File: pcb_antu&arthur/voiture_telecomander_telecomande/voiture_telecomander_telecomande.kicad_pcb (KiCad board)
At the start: 2 copper layers, 100 x 85 mm, 31 parts, among them J1 batterie, J2 Ecran 7 segments, J3 bouton1, J4 bouton2, J5 interrupteur, J6 led RGB, U1 ESP32-C6-DEVKITC-1-N8, U2 COM-09032 (joystick)

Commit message: mise a jour PCB antu_arthur
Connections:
- J6 pad 4: GND -> +3V3
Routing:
- net +3V3: track 177.7 -> 206.4 mm
- net GND: track 265.5 -> 261.3 mm
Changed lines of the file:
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@@
 		)
 		(embedded_fonts no)
-		(model "${KICAD9_3DMODEL_DIR}/Resistor_THT.3dshapes/R_Axial_DIN0207_L6.3mm_D2.5mm_P10.16mm_Horizontal.step"
+		(model "${KIPRJMOD}/3d/R_Axial_DIN0207_L6.3mm_D2.5mm_P10.16mm_Horizontal.step"
 			(offset
 				(xyz 0 0 0)
@@
 		)
 		(embedded_fonts no)
-		(model "${KICAD9_3DMODEL_DIR}/Resistor_THT.3dshapes/R_Axial_DIN0207_L6.3mm_D2.5mm_P10.16mm_Horizontal.step"
+		(model "${KIPRJMOD}/3d/R_Axial_DIN0207_L6.3mm_D2.5mm_P10.16mm_Horizontal.step"
 			(offset
 				(xyz 0 0 0)
@@
 		)
 		(embedded_fonts no)
-		(model "${KICAD9_3DMODEL_DIR}/Capacitor_THT.3dshapes/C_Radial_D4.0mm_H7.0mm_P1.50mm.step"
+		(model "${KIPRJMOD}/3d/C_Radial_D4.0mm_H7.0mm_P1.50mm.step"
 			(offset
 				(xyz 0 0 0)
@@
 		)
 		(embedded_fonts no)
-		(model "${KICAD9_3DMODEL_DIR}/Resistor_THT.3dshapes/R_Axial_DIN0207_L6.3mm_D2.5mm_P10.16mm_Horizontal.step"
+		(model "${KIPRJMOD}/3d/R_Axial_DIN0207_L6.3mm_D2.5mm_P10.16mm_Horizontal.step"
 			(offset
 				(xyz 0 0 0)
@@
 		)
 		(embedded_fonts no)
-		(model "${KICAD9_3DMODEL_DIR}/Resistor_THT.3dshapes/R_Axial_DIN0207_L6.3mm_D2.5mm_P10.16mm_Horizontal.step"
+		(model "${KIPRJMOD}/3d/R_Axial_DIN0207_L6.3mm_D2.5mm_P10.16mm_Horizontal.step"
 			(offset
 				(xyz 0 0 0)
@@
 		)
 		(embedded_fonts no)
-		(model "${KICAD9_3DMODEL_DIR}/Capacitor_THT.3dshapes/C_Radial_D4.0mm_H7.0mm_P1.50mm.step"
+		(model "${KIPRJMOD}/3d/C_Radial_D4.0mm_H7.0mm_P1.50mm.step"
 			(offset
 				(xyz 0 0 0)
@@
 		)
 		(embedded_fonts no)
-		(model "${KICAD9_3DMODEL_DIR}/Capacitor_THT.3dshapes/C_Radial_D4.0mm_H7.0mm_P1.50mm.step"
+		(model "${KIPRJMOD}/3d/C_Radial_D4.0mm_H7.0mm_P1.50mm.step"
 			(offset
 				(xyz 0 0 0)
@@
 		)
 		(embedded_fonts no)
-		(model "${KICAD9_3DMODEL_DIR}/Capacitor_THT.3dshapes/C_Radial_D4.0mm_H7.0mm_P1.50mm.step"
+		(model "${KIPRJMOD}/3d/C_Radial_D4.0mm_H7.0mm_P1.50mm.step"
 			(offset
 				(xyz 0 0 0)
@@
 		)
 		(embedded_fonts no)
-		(model "${KICAD9_3DMODEL_DIR}/Resistor_THT.3dshapes/R_Axial_DIN0207_L6.3mm_D2.5mm_P10.16mm_Horizontal.step"
+		(model "${KIPRJMOD}/3d/R_Axial_DIN0207_L6.3mm_D2.5mm_P10.16mm_Horizontal.step"
 			(offset
 				(xyz 0 0 0)
@@
 		)
 		(embedded_fonts no)
-		(model "${KICAD9_3DMODEL_DIR}/Connector_JST.3dshapes/JST_XH_B2B-XH-A_1x02_P2.50mm_Vertical.step"
+		(model "${KIPRJMOD}/3d/JST_XH_B2B-XH-A_1x02_P2.50mm_Vertical.step"
 			(offset
 				(xyz 0 0 0)
@@
 		)
 		(embedded_fonts no)
-		(model "${KICAD9_3DMODEL_DIR}/Resistor_THT.3dshapes/R_Axial_DIN0207_L6.3mm_D2.5mm_P10.16mm_Horizontal.step"
+		(model "${KIPRJMOD}/3d/R_Axial_DIN0207_L6.3mm_D2.5mm_P10.16mm_Horizontal.step"
 			(offset
 				(xyz 0 0 0)
@@
 		)
 		(embedded_fonts no)
-		(model "${KICAD9_3DMODEL_DIR}/Resistor_THT.3dshapes/R_Axial_DIN0207_L6.3mm_D2.5mm_P10.16mm_Horizontal.step"
+		(model "${KIPRJMOD}/3d/R_Axial_DIN0207_L6.3mm_D2.5mm_P10.16mm_Horizontal.step"
 			(offset
 				(xyz 0 0 0)
@@
 		)
 		(embedded_fonts no)
-		(model "${KICAD9_3DMODEL_DIR}/Resistor_THT.3dshapes/R_Axial_DIN0207_L6.3mm_D2.5mm_P10.16mm_Horizontal.step"
+		(model "${KIPRJMOD}/3d/R_Axial_DIN0207_L6.3mm_D2.5mm_P10.16mm_Horizontal.step"
 			(offset
 				(xyz 0 0 0)
@@
 		)
 		(embedded_fonts no)
-		(model "${KICAD9_3DMODEL_DIR}/Resistor_THT.3dshapes/R_Axial_DIN0207_L6.3mm_D2.5mm_P10.16mm_Horizontal.step"
+		(model "${KIPRJMOD}/3d/R_Axial_DIN0207_L6.3mm_D2.5mm_P10.16mm_Horizontal.step"
 			(offset
 				(xyz 0 0 0)
@@
 		)
 		(embedded_fonts no)
-		(model "${KICAD9_3DMODEL_DIR}/Resistor_THT.3dshapes/R_Axial_DIN0207_L6.3mm_D2.5mm_P10.16mm_Horizontal.step"
+		(model "${KIPRJMOD}/3d/R_Axial_DIN0207_L6.3mm_D2.5mm_P10.16mm_Horizontal.step"
 			(offset
 				(xyz 0 0 0)
@@
 		)
 		(embedded_fonts no)
-		(model "${KICAD9_3DMODEL_DIR}/Capacitor_THT.3dshapes/C_Radial_D4.0mm_H7.0mm_P1.50mm.step"
+		(model "${KIPRJMOD}/3d/C_Radial_D4.0mm_H7.0mm_P1.50mm.step"
 			(offset
 				(xyz 0 0 0)
@@
 		)
 		(embedded_fonts no)
-		(model "${KICAD9_3DMODEL_DIR}/Capacitor_THT.3dshapes/C_Radial_D4.0mm_H7.0mm_P1.50mm.step"
+		(model "${KIPRJMOD}/3d/C_Radial_D4.0mm_H7.0mm_P1.50mm.step"
 			(offset
 				(xyz 0 0 0)
@@
 		)
 		(embedded_fonts no)
-		(model "${KICAD9_3DMODEL_DIR}/Resistor_THT.3dshapes/R_Axial_DIN0207_L6.3mm_D2.5mm_P10.16mm_Horizontal.step"
+		(model "${KIPRJMOD}/3d/R_Axial_DIN0207_L6.3mm_D2.5mm_P10.16mm_Horizontal.step"
 			(offset
 				(xyz 0 0 0)
@@
 		)
 		(embedded_fonts no)
-		(model "${KICAD9_3DMODEL_DIR}/Connector_JST.3dshapes/JST_XH_B2B-XH-A_1x02_P2.50mm_Vertical.step"
+		(model "${KIPRJMOD}/3d/JST_XH_B2B-XH-A_1x02_P2.50mm_Vertical.step"
 			(offset
 				(xyz 0 0 0)
@@
 		)
 		(embedded_fonts no)
-		(model "${KICAD9_3DMODEL_DIR}/Resistor_THT.3dshapes/R_Axial_DIN0207_L6.3mm_D2.5mm_P10.16mm_Horizontal.step"
+		(model "${KIPRJMOD}/3d/R_Axial_DIN0207_L6.3mm_D2.5mm_P10.16mm_Horizontal.step"
 			(offset
 				(xyz 0 0 0)
@@
 		)
 		(embedded_fonts no)
-		(model "${KICAD9_3DMODEL_DIR}/Resistor_THT.3dshapes/R_Axial_DIN0207_L6.3mm_D2.5mm_P10.16mm_Horizontal.step"
+		(model "${KIPRJMOD}/3d/R_Axial_DIN0207_L6.3mm_D2.5mm_P10.16mm_Horizontal.step"
 			(offset
 				(xyz 0 0 0)
@@
 			(layers "*.Cu" "*.Mask")
 			(remove_unused_layers no)
-			(net 8 "GND")
+			(net 3 "+3V3")
 			(pinfunction "Pin_4")
 			(pintype "passive")
 		)
 		(embedded_fonts no)
-		(model "${KICAD9_3DMODEL_DIR}/Connector_PinSocket_2.54mm.3dshapes/PinSocket_1x04_P2.54mm_Vertical.step"
+		(model "${KIPRJMOD}/3d/PinSocket_1x04_P2.54mm_Vertical.step"
 			(offset
 				(xyz 0 0 0)
@@
 		)
 		(embedded_fonts no)
-		(model "${KICAD9_3DMODEL_DIR}/Capacitor_THT.3dshapes/C_Radial_D4.0mm_H7.0mm_P1.50mm.step"
+		(model "${KIPRJMOD}/3d/C_Radial_D4.0mm_H7.0mm_P1.50mm.step"
 			(offset
 				(xyz 0 0 0)
@@
 		)
 		(embedded_fonts no)
-		(model "${KICAD9_3DMODEL_DIR}/Connector_JST.3dshapes/JST_XH_B2B-XH-A_1x02_P2.50mm_Vertical.step"
+		(model "${KIPRJMOD}/3d/JST_XH_B2B-XH-A_1x02_P2.50mm_Vertical.step"
 			(offset
 				(xyz 0 0 0)
@@
 	)
 	(segment
+		(start 175.948 71.948)
+		(end 177.5 73.5)
+		(width 0.2)
+		(layer "F.Cu")
+		(net 3)
+	)
+	(segment
 		(start 120.95 133.42)
 		(end 122.051 132.319)
@@
 	)
 	(segment
+		(start 176.2019 66.849)
+		(end 175.948 67.1029)
+		(width 0.2)
+		(layer "F.Cu")
+		(net 3)
+	)
+	(segment
 		(start 112.85 133.42)
 		(end 113.951 132.319)
@@
 	)
 	(segment
+		(start 187.651 66.849)
+		(end 176.2019 66.849)
+		(width 0.2)
+		(layer "F.Cu")
+		(net 3)
+	)
+	(segment
 		(start 104.949 108.551)
 		(end 104.949 125.519)
@@
 	)
 	(segment
+		(start 186.5 75.62)
+		(end 187.651 74.469)
+		(width 0.2)
+		(layer "F.Cu")
+		(net 3)
+	)
+	(segment
 		(start 112.84 100.66)
 		(end 112.84 97.9155)
@@
 	)
 	(segment
+		(start 187.651 74.469)
+		(end 187.651 66.849)
+		(width 0.2)
+		(layer "F.Cu")
+		(net 3)
+	)
+	(segment
+		(start 175.948 67.1029)
+		(end 175.948 71.948)
+		(width 0.2)
+		(layer "F.Cu")
+		(net 3)
+	)
+	(segment
 		(start 152.249 132.319)
 		(end 153.35 133.42)
@@
 	)
 	(segment
+		(start 186.08 76.04)
+		(end 186.5 75.62)
+		(width 0.2)
+		(layer "B.Cu")
+		(net 3)
+	)
+	(segment
 		(start 183 143)
 		(end 186 140)
@@
 	)
 	(segment
-		(start 186.08 76.04)
-		(end 186.5 75.62)
-		(width 0.2)
-		(layer "B.Cu")
-		(net 8)
-	)
-	(segment
 		(start 178.475 107.75)
 		(end 177.975 108.25)
@@
 	)
 	(segment
-		(start 177.5 76.04)
-		(end 186.08 76.04)
+		(start 190.05 140)
+		(end 190.05 134.45)
 		(width 0.2)
 		(layer "B.Cu")
@@
 	)
 	(segment
-		(start 190.05 140)
-		(end 190.05 134.45)
+		(start 177.5 76.04)
+		(end 180.42 76.04)
 		(width 0.2)
 		(layer "B.Cu")
@@
 	)
 	(segment
-		(start 187.88 83.5)
-		(end 187.88 77)
-		(width 0.2)
-		(layer "B.Cu")
-		(net 8)
-	)
-	(segment
 		(start 123 83.8325)
 		(end 121.857 84.9755)
@@
 	)
 	(segment
-		(start 187.88 77)
-		(end 186.5 75.62)
-		(width 0.2)
-		(layer "B.Cu")
-		(net 8)
-	)
-	(segment
 		(start 183.599 139.099)
 		(end 184.5 140)
@@
 	)
 	(segment
+		(start 180.42 76.04)
+		(end 187.88 83.5)
+		(width 0.2)
+		(layer "B.Cu")
+		(net 8)
+	)
+	(segment
 		(start 179.68 90.5)
 		(end 191.08 90.5)
@@
 		(net 8)
 		(net_name "GND")
+		(locked yes)
 		(layer "B.Cu")
 		(hatch edge 0.5)

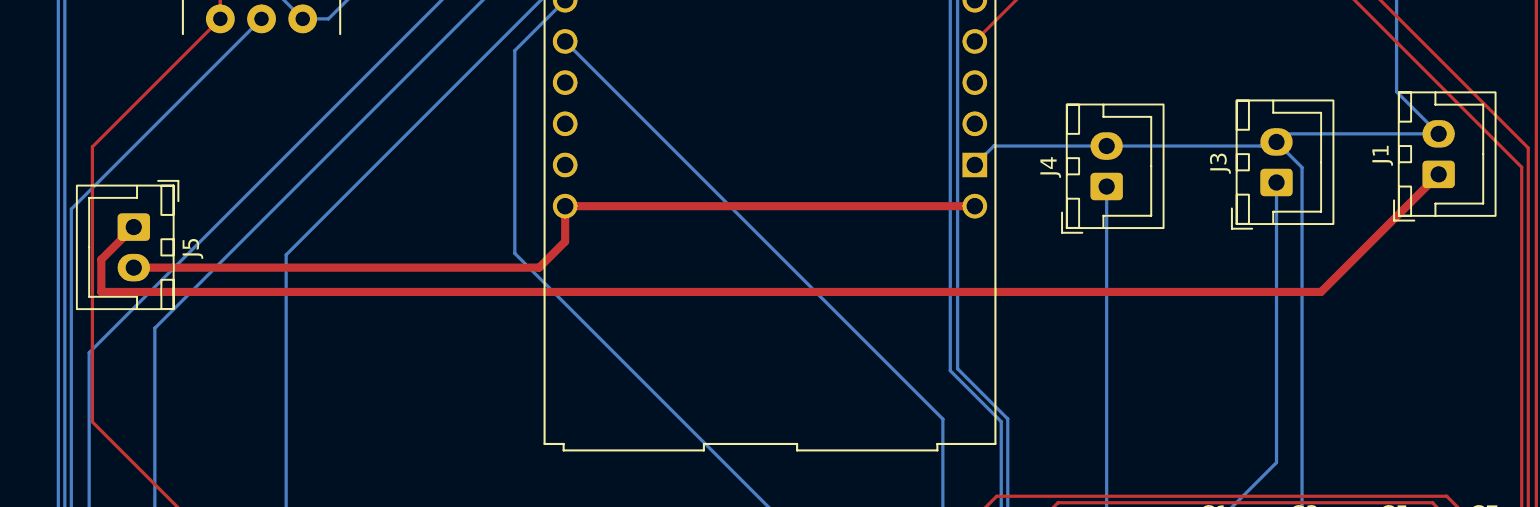
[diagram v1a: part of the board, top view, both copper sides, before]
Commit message: ajout d'un converter buck
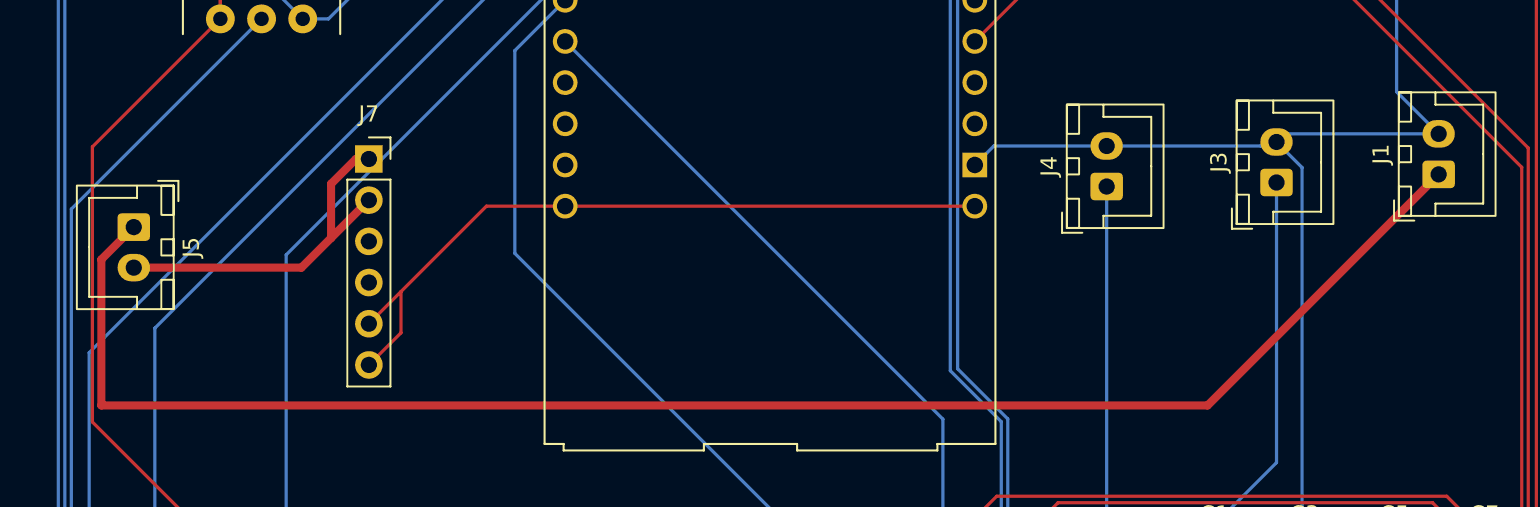
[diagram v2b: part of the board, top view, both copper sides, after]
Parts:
- added J7: Conn_01x06_Socket, Connector_PinSocket_2.54mm:PinSocket_1x06_P2.54mm_Vertical, F.Cu at (122.0, 109.3)
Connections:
- J5 pad 2: /Alim_ESP -> +BATT
- U1 pad J1_15: /Alim_ESP -> +5V
- U1 pad J3_15: /Alim_ESP -> +5V
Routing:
- net /Alim_ESP: track 54.7 -> 0.00 mm
- net +5V: track 0.00 -> 45.7 mm
- net +BATT: track 0.00 -> 22.5 mm
- net /B+: track 90.3 -> 100.2 mm

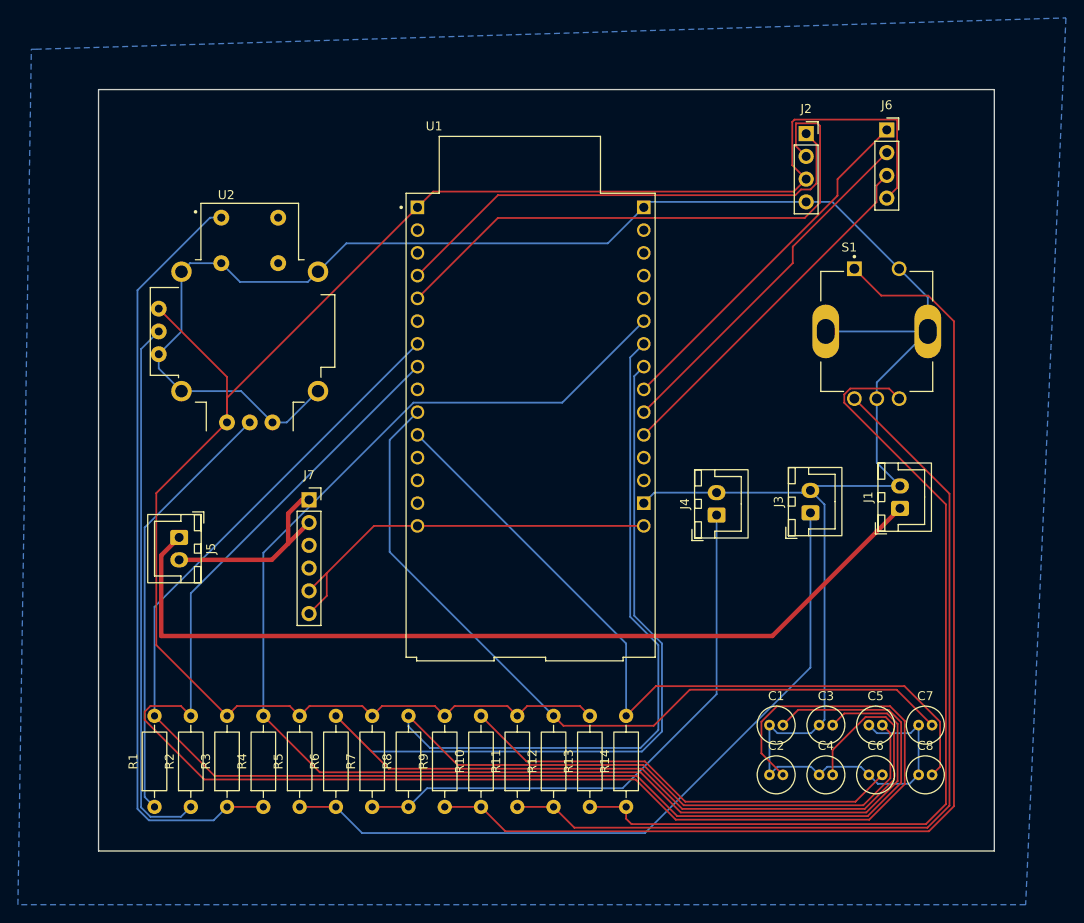
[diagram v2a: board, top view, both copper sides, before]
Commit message: déplacement composant
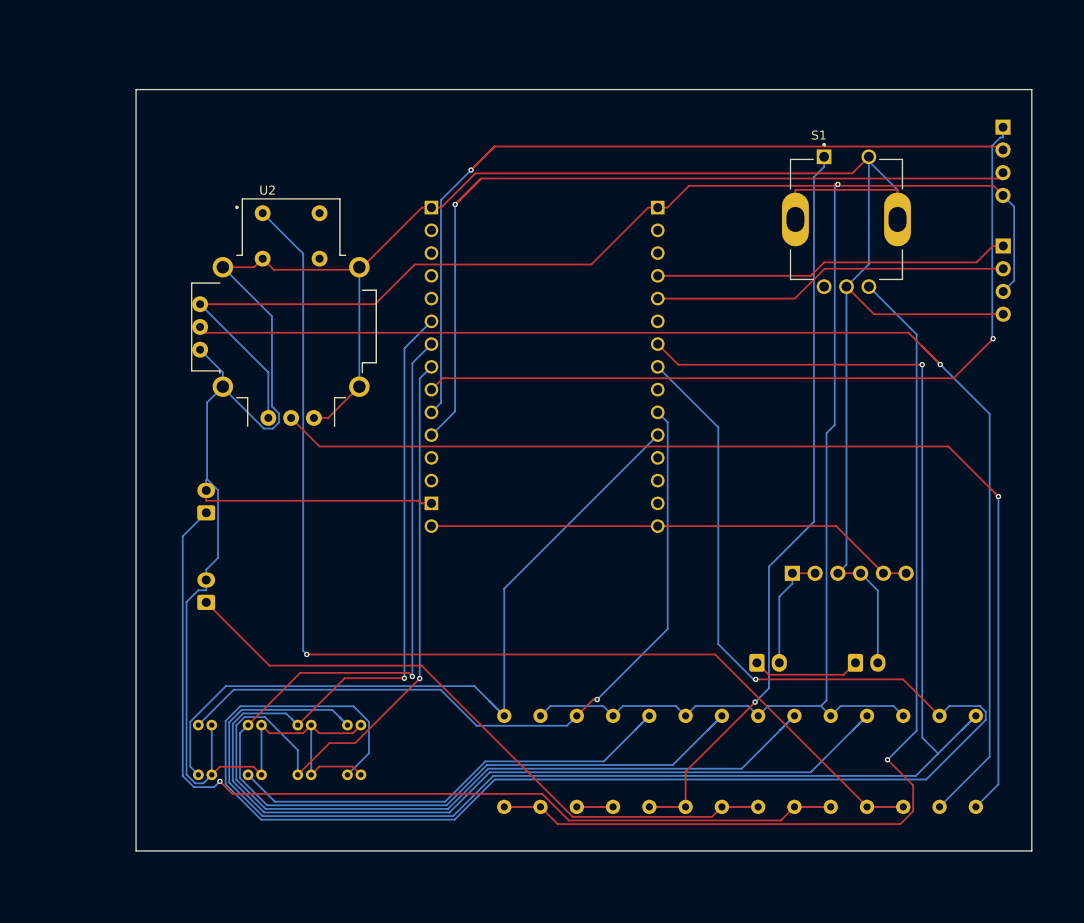
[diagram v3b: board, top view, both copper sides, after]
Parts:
- C1, C2, C3, C4, C5, C6, C7, C8, J1, J2, J3, J4, J5, J6, J7, R1, R10, R11, R12, R13, R14, R2, R3, R4, R5, R6, R7, R8, R9, U1: moved to B.Cu
- moved R1 91.7 mm to (196.4, 143.6)
- moved R2 83.6 mm to (192.4, 143.6)
- moved C7 78.9 mm to (111.1, 134.4), turned to 180 degrees
- moved C8 78.9 mm to (111.1, 140.0), turned to 180 degrees
- moved R3 75.5 mm to (188.3, 143.6)
- moved C5 67.8 mm to (116.7, 134.4), turned to 180 degrees
- moved C6 67.8 mm to (116.7, 140.0), turned to 180 degrees
- moved J3 67.4 mm to (110.5, 110.8)
- moved R4 67.4 mm to (184.3, 143.6)
- moved J5 66.0 mm to (172.0, 127.5), turned to 0 degrees
- moved R5 59.3 mm to (180.2, 143.6)
- moved J4 57.8 mm to (110.5, 120.8)
- moved C3 56.7 mm to (122.2, 134.4), turned to 180 degrees
- moved C4 56.7 mm to (122.2, 140.0), turned to 180 degrees
- moved J7 54.6 mm to (176.0, 117.5), turned to -90 degrees
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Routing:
- net GND: track 261.3 -> 357.6 mm
- net Net-(R11-Pad1): track 100.1 -> 8.10 mm
- net Net-(U2-V): track 60.4 -> 149.8 mm, vias 0 -> 1
- net /B+: track 100.2 -> 12.1 mm
- net Net-(U2-H): track 48.2 -> 120.4 mm, vias 0 -> 1
- net /B: track 40.2 -> 105.6 mm, vias 0 -> 1
- net /G: track 40.2 -> 104.3 mm, vias 0 -> 1
- net /R: track 40.2 -> 89.4 mm, vias 0 -> 1
- net Net-(U2-SEL+): track 85.8 -> 129.0 mm, vias 0 -> 1
- net Net-(R10-Pad1): track 126.8 -> 87.1 mm, vias 0 -> 1
- net Net-(J3-Pin_1): track 83.2 -> 110.1 mm, vias 0 -> 1
- net /bouton1: track 167.0 -> 141.2 mm, vias 0 -> 1
- net /DIO_ECRAN: track 64.9 -> 40.0 mm
- net /pot_y: track 164.4 -> 188.8 mm, vias 0 -> 1
- net +3V3: track 206.4 -> 229.6 mm, vias 0 -> 1
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- removed copper zone on B.Cu, net GND
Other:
- board text added: "${REFERENCE}"
